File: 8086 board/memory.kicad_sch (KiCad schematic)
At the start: 43 parts, among them U10 74AC573, U11 74HC138, U12 74HC138, U13 IS61C6416AL, U2 74HC32, U39 29F800BA, U40 IS61C6416AL, U8 74AC573, U9 74AC573

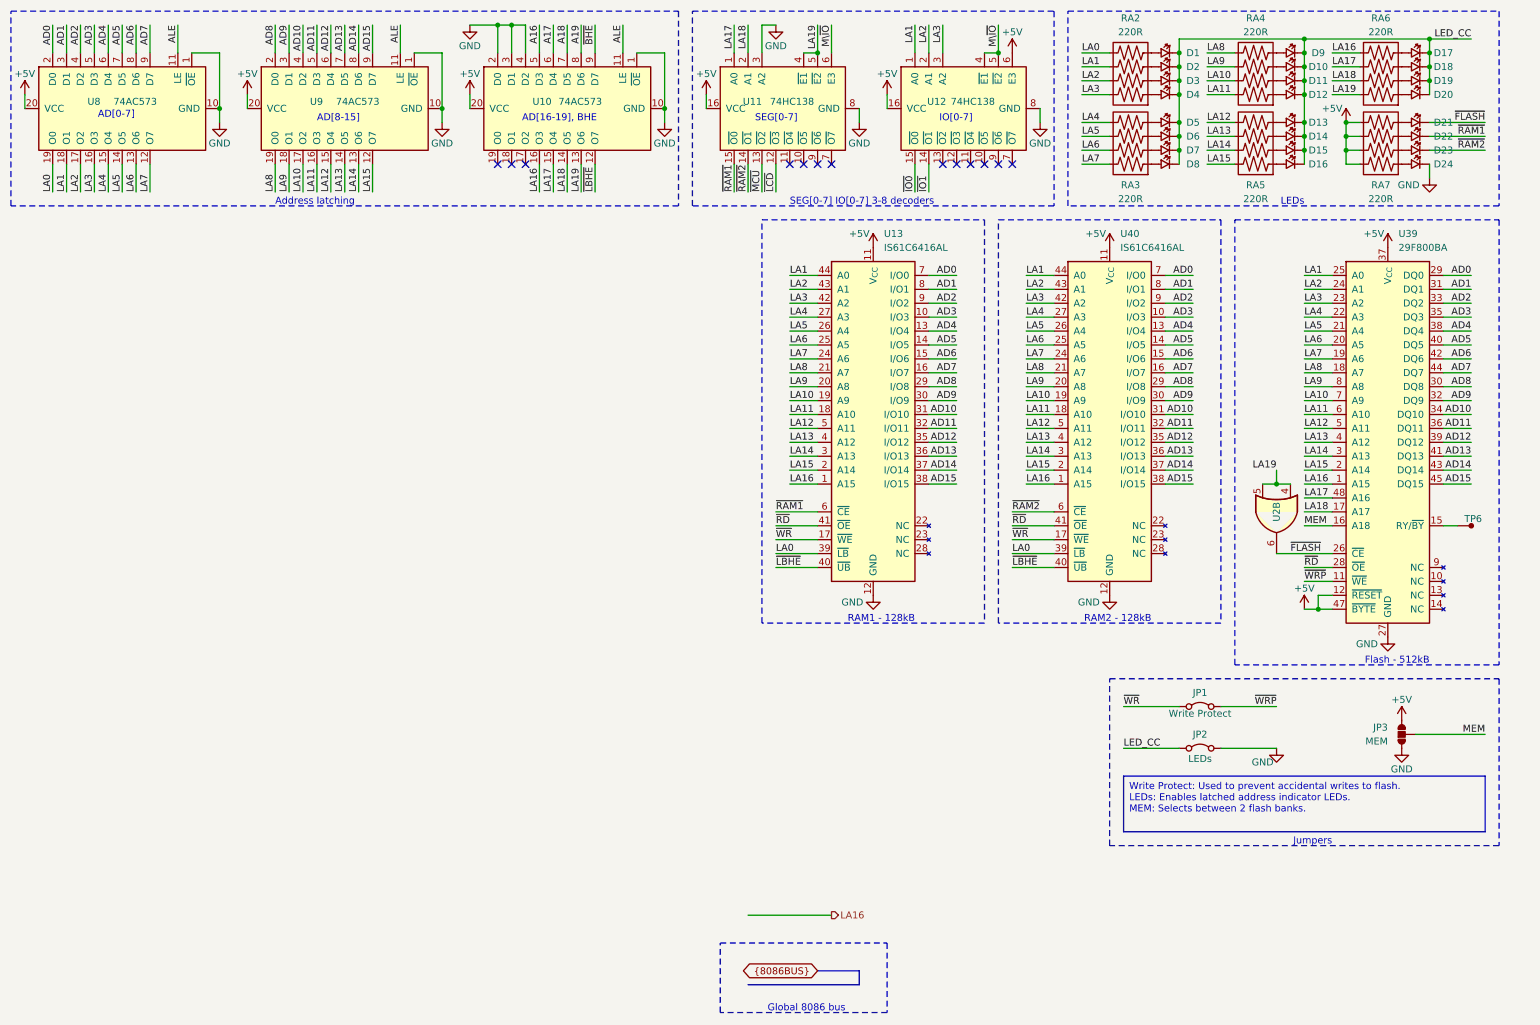
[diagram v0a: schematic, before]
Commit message: PCB: more layout work. some schematic changes.
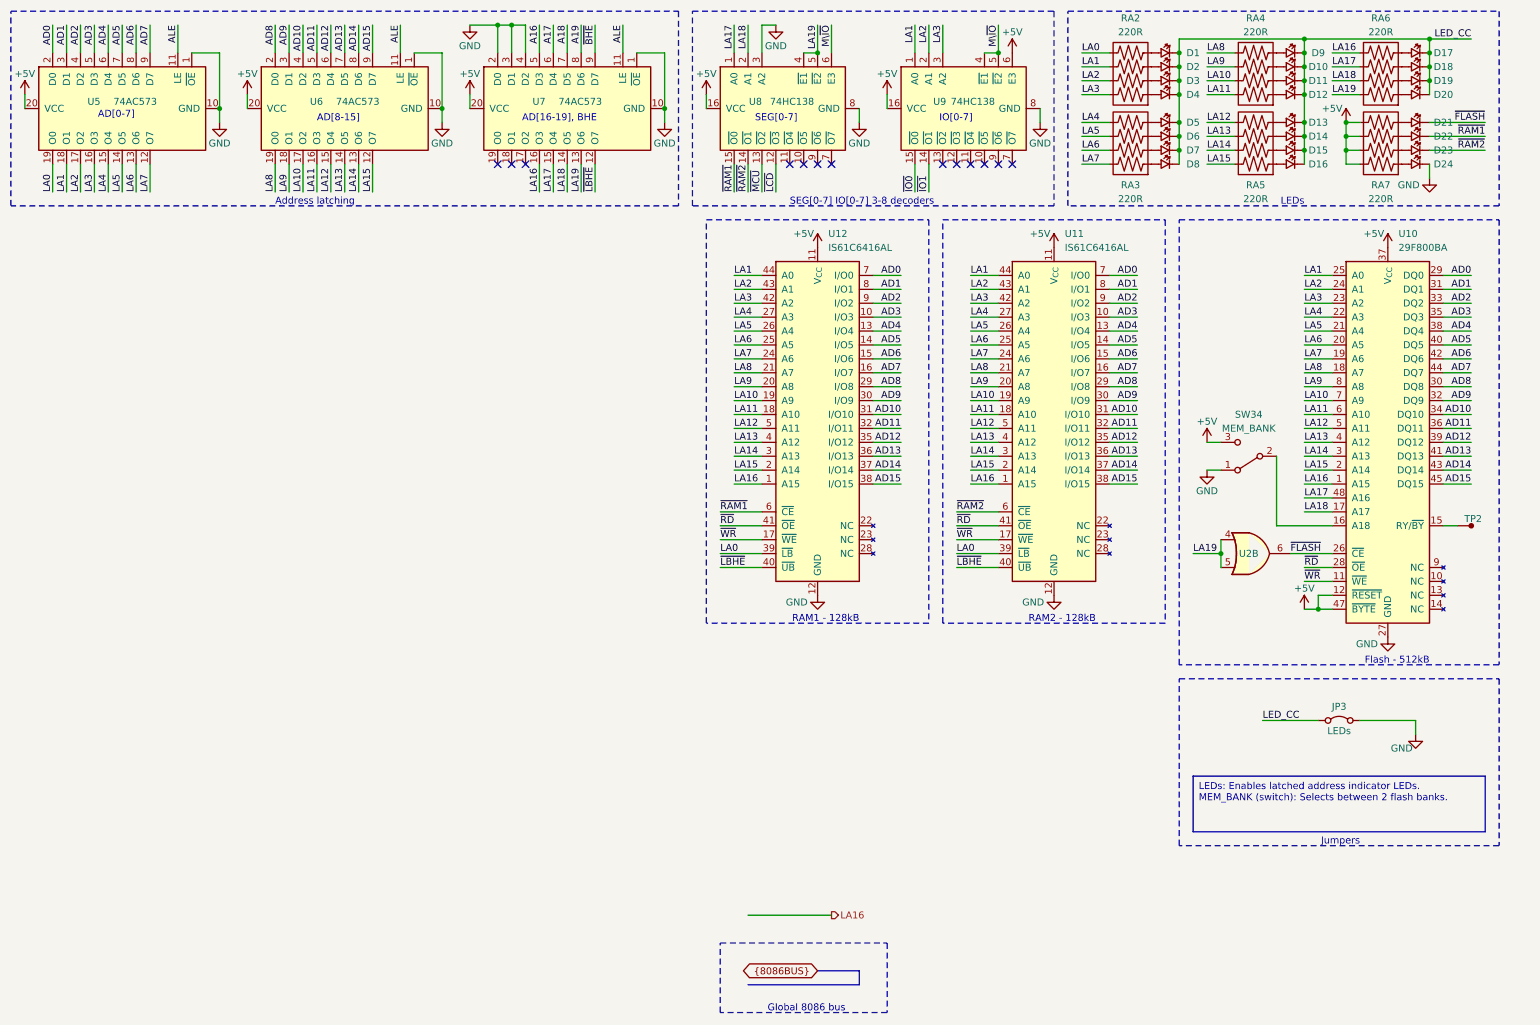
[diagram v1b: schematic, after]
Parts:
- removed JP1: Write Protect, Jumper:SolderJumper-2_P1.3mm_Open_TrianglePad1.0x1.5mm, symbol 8086PC:Jumper_2_Bridged
- removed JP3: MEM, Jumper:SolderJumper-3_P2.0mm_Open_TrianglePad1.0x1.5mm, symbol 8086PC:SolderJumper
- added SW34: MEM_BANK, Button_Switch_SMD:SW_SPDT_PCM12, symbol Switch:SW_SPDT
- JP3: renamed from JP2; footprint Jumper:SolderJumper-2_P1.3mm_Open_TrianglePad1.0x1.5mm -> Jumper:SolderJumper-2_P1.3mm_Bridged_RoundedPad1.0x1.5mm
- renumbered TP6 to TP2, U39 to U10, U40 to U11, U13 to U12, U8 to U5, U9 to U6, U10 to U7, U11 to U8, U12 to U9
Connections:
- net ~{WRP} is gone; now on net ~{WR}: U10.11 (~{WE})
- net +5V: now also SW34.3 (C)
- net GND: now also SW34.1 (A)
- net MEM: no longer names the net of U10.16 (A18)
- net MEM: now also SW34.2 (B)
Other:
- moved on the sheet: JP3, U11, U12, U2B

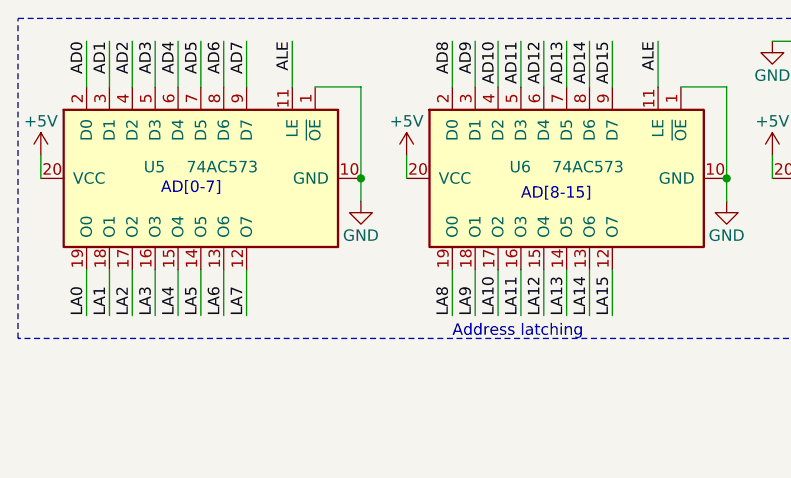
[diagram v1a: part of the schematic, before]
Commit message: PCB: different layout
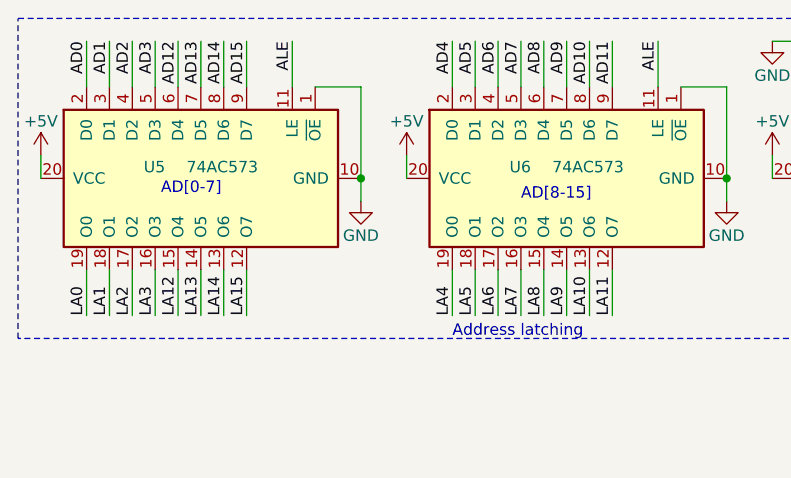
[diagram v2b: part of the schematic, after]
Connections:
- net AD10: now also U6.8 (D6); no longer U6.4 (D2)
- net AD11: now also U6.9 (D7); no longer U6.5 (D3)
- net AD12: now also U5.6 (D4); no longer U6.6 (D4)
- net AD13: now also U5.7 (D5); no longer U6.7 (D5)
- net AD14: now also U5.8 (D6); no longer U6.8 (D6)
- net AD15: now also U5.9 (D7); no longer U6.9 (D7)
- net AD4: now also U6.2 (D0); no longer U5.6 (D4)
- net AD5: now also U6.3 (D1); no longer U5.7 (D5)
- net AD6: now also U6.4 (D2); no longer U5.8 (D6)
- net AD7: now also U6.5 (D3); no longer U5.9 (D7)
- net AD8: now also U6.6 (D4); no longer U6.2 (D0)
- net AD9: now also U6.7 (D5); no longer U6.3 (D1)
- net LA10: now also U6.13 (O6); no longer U6.17 (O2)
- net LA11: now also U6.12 (O7); no longer U6.16 (O3)
- net LA12: now also U5.15 (O4); no longer U6.15 (O4)
- net LA13: now also U5.14 (O5); no longer U6.14 (O5)
- net LA14: now also U5.13 (O6); no longer U6.13 (O6)
- net LA15: now also U5.12 (O7); no longer U6.12 (O7)
- net LA4: now also U6.19 (O0); no longer U5.15 (O4)
- net LA5: now also U6.18 (O1); no longer U5.14 (O5)
- net LA6: now also U6.17 (O2); no longer U5.13 (O6)
- net LA7: now also U6.16 (O3); no longer U5.12 (O7)
- net LA8: now also U6.15 (O4); no longer U6.19 (O0)
- net LA9: now also U6.14 (O5); no longer U6.18 (O1)

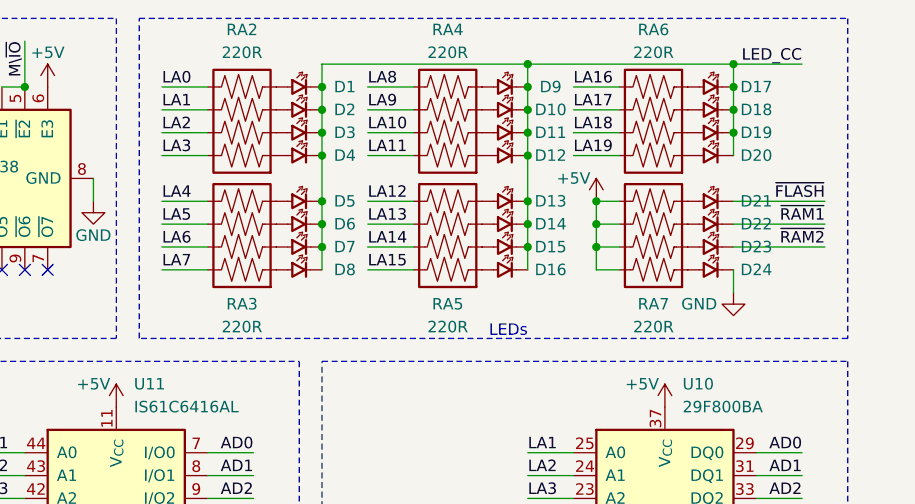
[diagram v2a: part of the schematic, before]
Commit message: PCB: layout and routing of IO, shift registers, and MCU
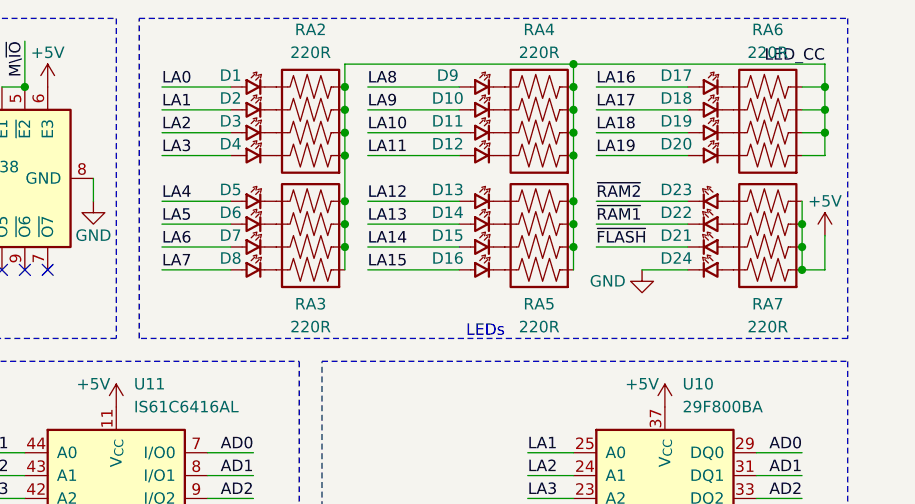
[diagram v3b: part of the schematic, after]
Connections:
- net +5V: now also RA7.1, RA7.2, RA7.3, RA7.4; no longer RA7.5, RA7.6, RA7.7, RA7.8
- net LA0: now also D1.1 (A); no longer RA2.5
- net LA1: now also D2.1 (A); no longer RA2.6
- net LA10: now also D11.1 (A); no longer RA4.7
- net LA11: now also D12.1 (A); no longer RA4.8
- net LA12: now also D13.1 (A); no longer RA5.5
- net LA13: now also D14.1 (A); no longer RA5.6
- net LA14: now also D15.1 (A); no longer RA5.7
- net LA15: now also D16.1 (A); no longer RA5.8
- net LA16: now also D17.1 (A); no longer RA6.5
- net LA17: now also D18.1 (A); no longer RA6.6
- net LA18: now also D19.1 (A); no longer RA6.7
- net LA19: now also D20.1 (A); no longer RA6.8
- net LA2: now also D3.1 (A); no longer RA2.7
- net LA3: now also D4.1 (A); no longer RA2.8
- net LA4: now also D5.1 (A); no longer RA3.5
- net LA5: now also D6.1 (A); no longer RA3.6
- net LA6: now also D7.1 (A); no longer RA3.7
- net LA7: now also D8.1 (A); no longer RA3.8
- net LA8: now also D9.1 (A); no longer RA4.5
- net LA9: now also D10.1 (A); no longer RA4.6
- net LED_CC: now also RA2.1, RA2.2, RA2.3, RA2.4, RA3.1, RA3.2, RA3.3, RA3.4, RA4.1, RA4.2, RA4.3, RA4.4, RA5.1, RA5.2, RA5.3, RA5.4, RA6.1, RA6.2, RA6.3, RA6.4; no longer D1.2 (K), D10.2 (K), D11.2 (K), D12.2 (K), D13.2 (K), D14.2 (K), D15.2 (K), D16.2 (K), D17.2 (K), D18.2 (K), D19.2 (K), D2.2 (K), D20.2 (K), D3.2 (K), D4.2 (K), D5.2 (K), D6.2 (K), D7.2 (K), D8.2 (K), D9.2 (K)
- net at D23.1 (A): now also RA7.5; no longer RA7.2
- net at D21.1 (A): now also RA7.7; no longer RA7.4
- net at D22.1 (A): now also RA7.6; no longer RA7.3
- net at D24.1 (A): now also RA7.8; no longer RA7.1
- new net: D1.2 (K), RA2.5
- new net: D2.2 (K), RA2.6
- new net: D3.2 (K), RA2.7
- new net: D4.2 (K), RA2.8
- new net: D19.2 (K), RA6.7
- new net: D8.2 (K), RA3.8
- new net: D20.2 (K), RA6.8
- new net: D12.2 (K), RA4.8
- new net: D5.2 (K), RA3.5
- new net: D6.2 (K), RA3.6
- new net: D7.2 (K), RA3.7
- new net: D17.2 (K), RA6.5
- new net: D18.2 (K), RA6.6
- new net: D15.2 (K), RA5.7
- new net: D11.2 (K), RA4.7
- new net: D10.2 (K), RA4.6
- new net: D16.2 (K), RA5.8
- new net: D13.2 (K), RA5.5
- new net: D14.2 (K), RA5.6
- new net: D9.2 (K), RA4.5
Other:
- moved on the sheet: D1, D10, D11, D12, D13, D14, D15, D16, D2, D21, D23, D3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

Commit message: small schematic  changes to better fit PCB
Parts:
- D21: value FLASH -> MCU
- D22: renamed from D24; value POWER -> LCD
- RA2, RA3, RA4, RA5, RA6, RA7: value 220R -> 1k
- SW34: footprint Button_Switch_SMD:SW_SPDT_PCM12 -> 8086PC:SW_SPDT_PCM12
- TP2: footprint TestPoint:TestPoint_Pad_1.5x1.5mm -> TestPoint:TestPoint_Pad_1.0x1.0mm
- renumbered D22 to D24
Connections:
- net +5V: now also SW34.1 (A); no longer SW34.3 (C)
- net A16: now also U7.2 (D0); no longer U7.5 (D3)
- net A17: now also U7.3 (D1); no longer U7.6 (D4)
- net A18: now also U7.4 (D2); no longer U7.7 (D5)
- net A19: now also U7.5 (D3); no longer U7.8 (D6)
- net AD0: now also U6.2 (D0); no longer U5.2 (D0)
- net AD1: now also U6.3 (D1); no longer U5.3 (D1)
- net AD10: now also U5.4 (D2); no longer U6.8 (D6)
- net AD11: now also U5.5 (D3); no longer U6.9 (D7)
- net AD2: now also U6.4 (D2); no longer U5.4 (D2)
- net AD3: now also U6.5 (D3); no longer U5.5 (D3)
- net AD4: now also U6.6 (D4); no longer U6.2 (D0)
- net AD5: now also U6.7 (D5); no longer U6.3 (D1)
- net AD6: now also U6.8 (D6); no longer U6.4 (D2)
- net AD7: now also U6.9 (D7); no longer U6.5 (D3)
- net AD8: now also U5.2 (D0); no longer U6.6 (D4)
- net AD9: now also U5.3 (D1); no longer U6.7 (D5)
- net GND: now also SW34.3 (C), U7.7 (D5), U7.8 (D6), U7.9 (D7); no longer D22.2 (K), SW34.1 (A), U7.2 (D0), U7.3 (D1), U7.4 (D2)
- net LA0: now also U6.19 (O0); no longer U5.19 (O0)
- net LA1: now also U6.18 (O1); no longer U5.18 (O1)
- net LA10: now also U5.17 (O2); no longer U6.13 (O6)
- net LA11: now also U5.16 (O3); no longer U6.12 (O7)
- net LA16: now also U7.19 (O0); no longer U7.16 (O3)
- net LA17: now also U7.18 (O1); no longer U7.15 (O4)
- net LA18: now also U7.17 (O2); no longer U7.14 (O5)
- net LA19: now also U7.16 (O3); no longer U7.13 (O6)
- net LA2: now also U6.17 (O2); no longer U5.17 (O2)
- net LA3: now also U6.16 (O3); no longer U5.16 (O3)
- net LA4: now also U6.15 (O4); no longer U6.19 (O0)
- net LA5: now also U6.14 (O5); no longer U6.18 (O1)
- net LA6: now also U6.13 (O6); no longer U6.17 (O2)
- net LA7: now also U6.12 (O7); no longer U6.16 (O3)
- net LA8: now also U5.19 (O0); no longer U6.15 (O4)
- net LA9: now also U5.18 (O1); no longer U6.14 (O5)
- net ~{BHE}: now also U7.6 (D4); no longer U7.9 (D7)
- net ~{FLASH}: no longer D21.2 (K)
- net ~{LBHE}: now also U7.15 (O4); no longer U7.12 (O7)
- net ~{LCD}: now also D22.2 (K)
- net ~{MCU}: now also D21.2 (K)
- net at D23.1 (A): now also RA7.6; no longer RA7.5
- net at D21.1 (A): now also RA7.8; no longer RA7.7
- net at D24.1 (A): now also RA7.5; no longer RA7.6
- net at D22.1 (A): now also RA7.7; no longer RA7.8
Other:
- moved on the sheet: D21, D22, D23, D24, SW34
